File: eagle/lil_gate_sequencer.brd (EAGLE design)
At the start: 100 x 80 mm, 68 parts, among them IC1 4093N, IC2 4017N, Q1 2N3904, Q2 2N3904

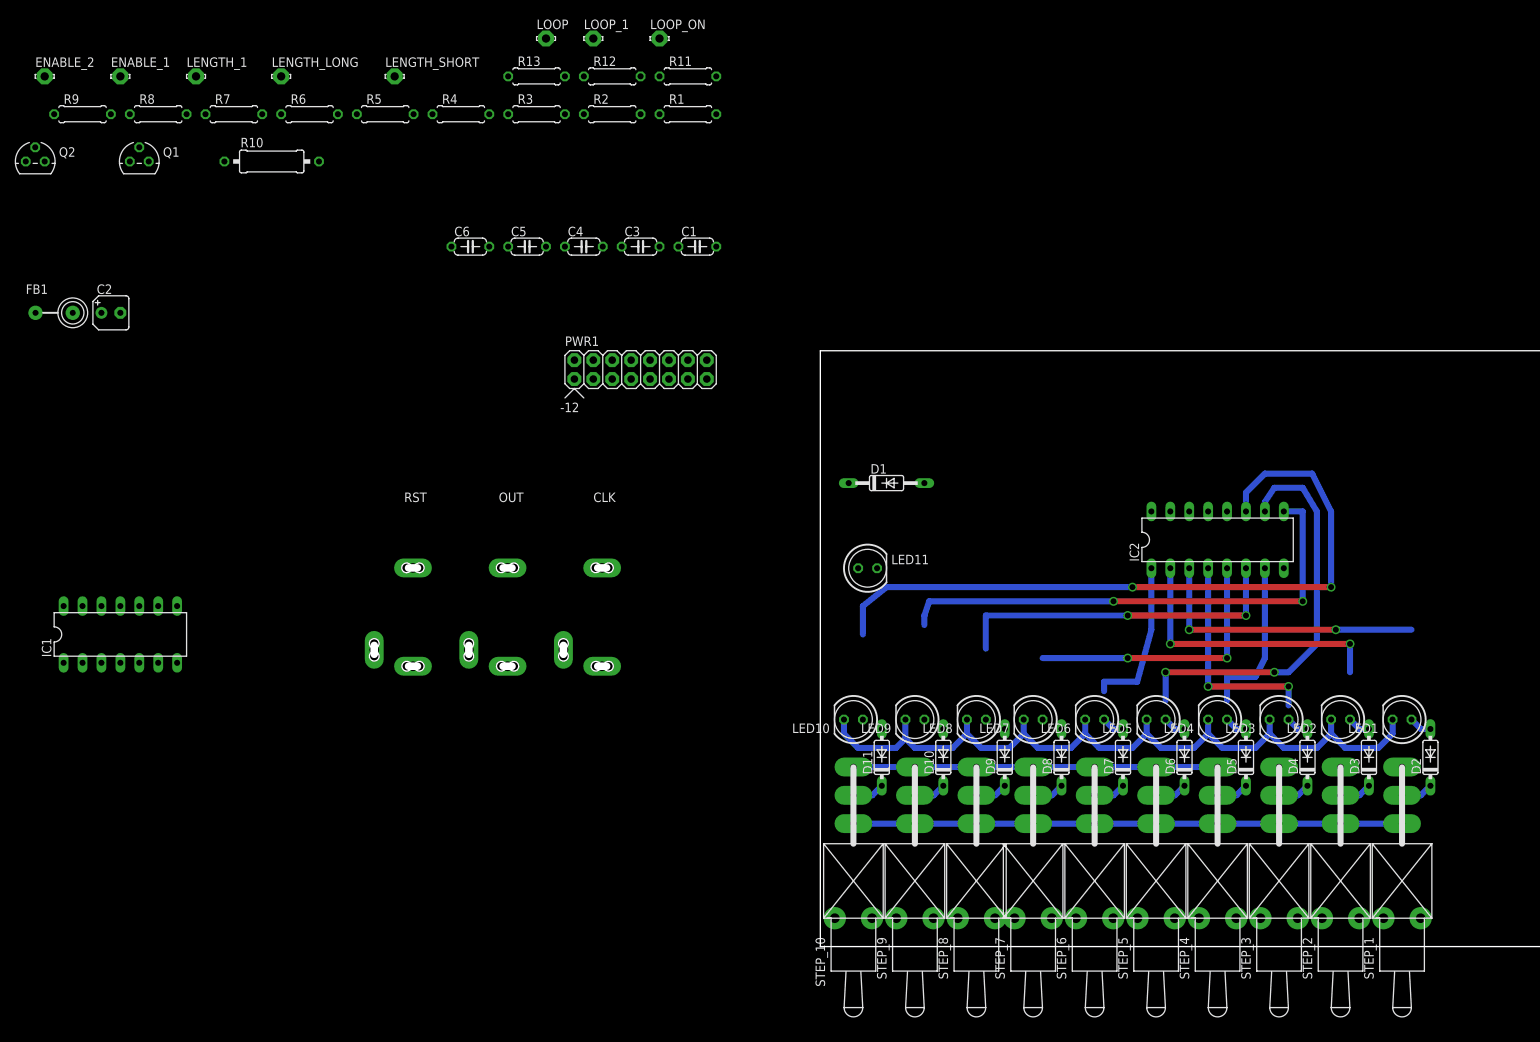
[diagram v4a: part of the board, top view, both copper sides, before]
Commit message: 4017 routed and adjusted
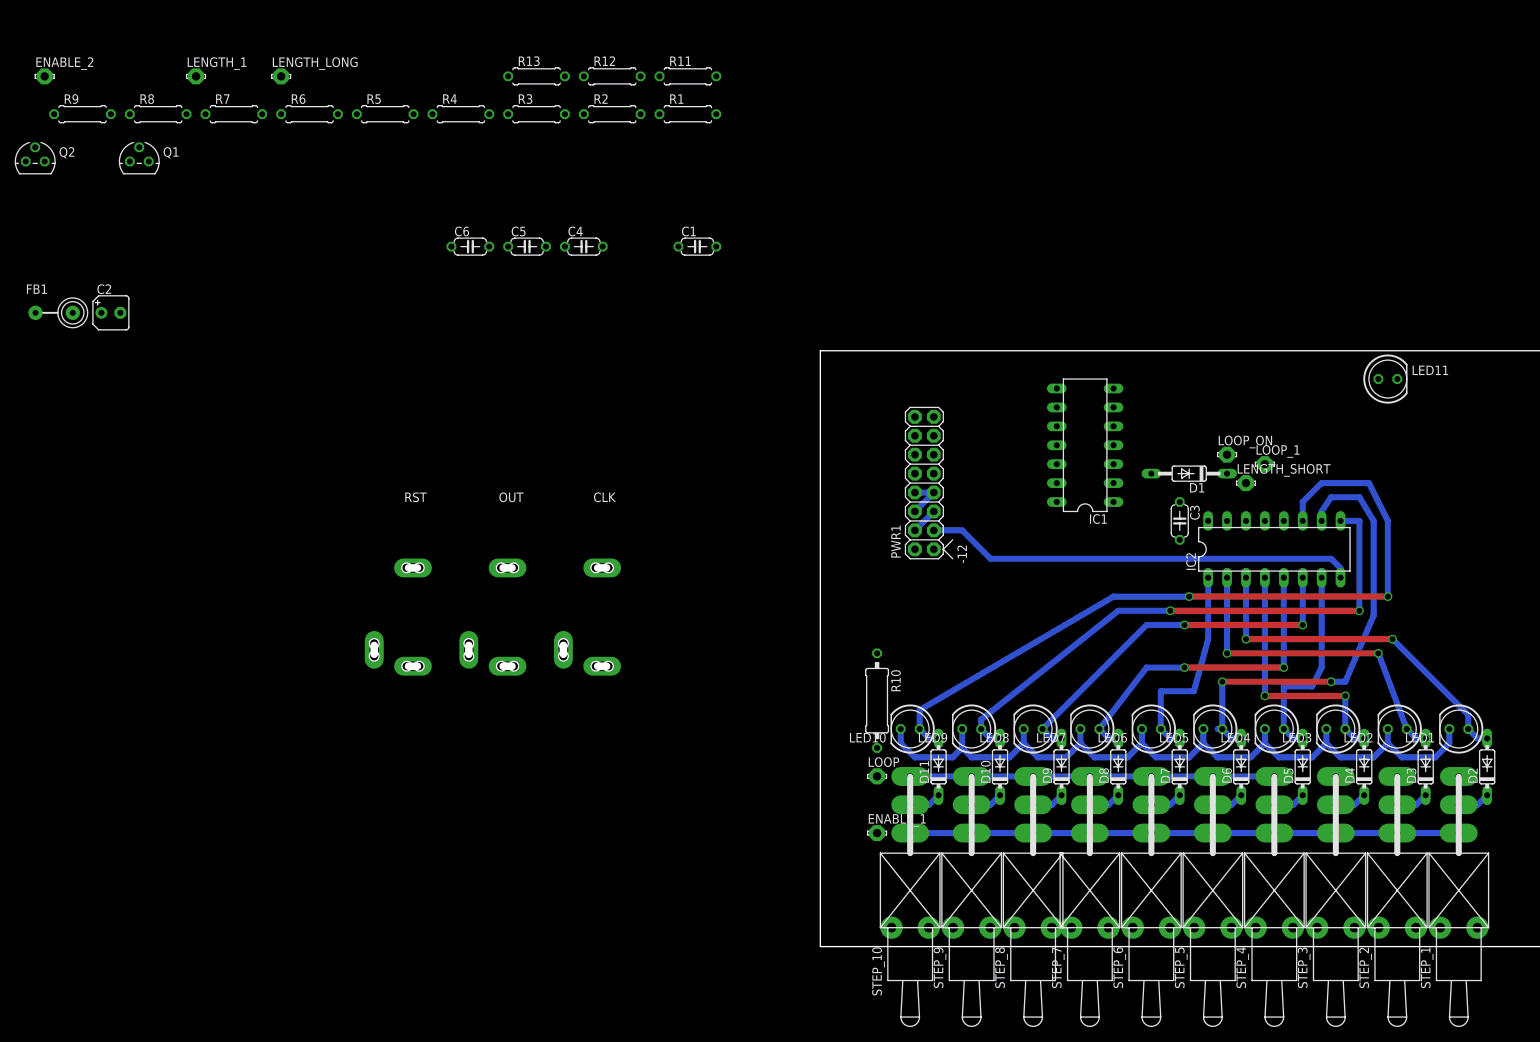
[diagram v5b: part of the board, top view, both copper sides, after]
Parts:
- moved ENABLE_1 143.7 mm to (7.62, 15.2)
- moved IC1 132.0 mm to (35.6, 67.3), turned to 90 degrees
- moved LENGTH_SHORT 126.7 mm to (57.1, 62.2)
- moved R10 108.8 mm to (7.62, 33.0), turned to 270 degrees
- moved LOOP 108.6 mm to (7.62, 22.9)
- moved LOOP_1 106.8 mm to (59.7, 64.8)
- moved LOOP_ON 94.5 mm to (54.6, 66.0)
- moved C3 81.2 mm to (48.3, 57.1), turned to 270 degrees
- moved LED11 74.3 mm to (76.2, 76.2)
- moved PWR1 44.4 mm to (14.0, 59.7), turned to 90 degrees
- moved D1 40.7 mm to (49.5, 63.5), turned to 180 degrees
- moved D3 7.73 mm to (81.3, 24.1)
- moved D4 7.73 mm to (73.0, 24.1)
- moved D8 7.73 mm to (40.0, 24.1)
- moved LED2 7.73 mm to (77.5, 29.2)
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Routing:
- net GND: track 0.00 -> 67.7 mm
- net N$27: track 36.8 -> 44.0 mm
- net N$31: track 68.0 -> 74.8 mm
- net N$15: track 41.2 -> 47.3 mm
- net N$33: track 95.9 -> 100.9 mm
- net N$29: track 45.7 -> 50.1 mm
- net N$25: track 24.3 -> 28.1 mm
- net N$17: track 41.2 -> 44.4 mm
- net N$21: track 25.0 -> 27.5 mm
- net N$23: track 57.6 -> 60.0 mm
- net N$19: track 32.3 -> 34.2 mm

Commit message: more routes
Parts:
- R10: device rcl:0309/12 -> rcl:0207/7
- moved Q2 177.5 mm to (69.8, 77.5), turned to 180 degrees
- moved R9 172.5 mm to (67.3, 66.0), turned to 180 degrees
- moved Q1 172.2 mm to (76.2, 66.0), turned to 180 degrees
- moved RST 162.0 mm to (100.3, 78.7), turned to 270 degrees
- moved R8 157.7 mm to (63.5, 71.1), turned to 180 degrees
- moved R7 139.9 mm to (55.9, 73.7)
- moved ENABLE_2 138.6 mm to (27.9, 74.9)
- moved CLK 135.3 mm to (100.3, 67.3), turned to 270 degrees
- moved LENGTH_LONG 132.8 mm to (50.8, 67.3)
- moved R4 130.7 mm to (77.5, 76.2), turned to 180 degrees
- moved R3 127.8 mm to (81.3, 66.0), turned to 270 degrees
- moved FB1 126.3 mm to (20.3, 57.1)
- moved R6 122.5 mm to (47.0, 71.1), turned to 270 degrees
- moved C2 118.1 mm to (20.3, 61.0)
- moved R1 116.0 mm to (83.8, 55.9)
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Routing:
- net GND: track 67.7 -> 440.3 mm
- net +12V: track 0.00 -> 50.8 mm
- net N$12: track 0.00 -> 31.6 mm
- net N$11: track 0.00 -> 26.2 mm
- net N$10: track 0.00 -> 22.4 mm
- net N$9: track 0.00 -> 17.1 mm
- net N$4: track 0.00 -> 13.1 mm
- net N$38: track 0.00 -> 12.5 mm
- net N$42: track 0.00 -> 11.2 mm
- net N$41: track 0.00 -> 11.0 mm
- net N$14: track 0.00 -> 10.5 mm
- net N$3: track 0.00 -> 7.92 mm
- net N$7: track 0.00 -> 7.67 mm
- net N$1: track 0.00 -> 7.66 mm
- net N$5: track 0.00 -> 6.88 mm
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
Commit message: routed
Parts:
- removed LED11: (no value), led:LED5MM
- added JP1: M02LOCK_LONGPADS, SparkFun-Connectors:1X02_LOCK_LONGPADS
- added OUT_LED, OUT_LED1: LSP11, solpad:LSP11
- moved OUT 72.7 mm to (6.35, 0.00), turned to 180 degrees
- moved CLK 67.3 mm to (100.3, 0.00), turned to 180 degrees
- moved R1 34.5 mm to (94.0, 22.9), turned to 270 degrees
- moved R13 21.1 mm to (8.89, 41.9), turned to 0 degrees
- moved C3 17.3 mm to (49.5, 53.3), turned to 270 degrees
- moved LENGTH_SHORT 11.5 mm to (47.0, 59.7)
- moved C4 11.4 mm to (25.4, 74.9), turned to 90 degrees
- moved C2 6.35 mm to (25.4, 57.1), turned to 90 degrees
- moved LOOP_ON 5.08 mm to (59.7, 66.0)
- moved FB1 4.02 mm to (19.1, 53.3)
- moved LENGTH_1 2.84 mm to (20.3, 74.9)
- moved LOOP_1 2.84 mm to (59.7, 61.0)
- moved C1 2.84 mm to (50.8, 74.9), turned to 270 degrees
- moved ENABLE_1 2.54 mm to (7.62, 17.8)
- moved PWR1 2.54 mm to (8.89, 53.3)
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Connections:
- new net N$39: JP1.1, PWR1.15, PWR1.16
- net N$43: now also OUT_LED1.MP; no longer LED11.K
- net N$6: now also JP1.2, OUT_LED.MP; no longer LED11.A
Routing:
- net N$6: track 0.00 -> 93.9 mm, vias 0 -> 2
- net N$5: track 6.88 -> 81.1 mm
- net N$4: track 13.1 -> 42.8 mm
- net +12V: track 50.8 -> 73.3 mm, vias 0 -> 2
- net N$34: track 48.9 -> 70.5 mm
- net N$39: track 0.00 -> 8.55 mm
- net N$36: track 73.7 -> 78.8 mm
- net N$41: track 11.0 -> 6.43 mm
- net N$43: track 0.00 -> 4.34 mm
- net GND: track 440.3 -> 436.1 mm, vias 0 -> 2
- net N$7: track 7.67 -> 4.02 mm
- net N$11: track 26.2 -> 22.7 mm
- net N$1: track 7.66 -> 10.5 mm
- net N$21: track 27.5 -> 24.9 mm
- net N$25: track 28.1 -> 26.0 mm
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
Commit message: reversed
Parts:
- moved LOOP 84.6 mm to (92.1, 27.3)
- moved ENABLE_1 83.8 mm to (91.4, 19.1)
- moved D2 74.3 mm to (15.2, 26.7)
- moved LED1 74.3 mm to (11.4, 31.8)
- moved STEP_1 74.3 mm to (11.4, 5.08)
- moved D11 73.7 mm to (89.5, 26.7)
- moved LED10 73.7 mm to (85.7, 31.8)
- moved STEP_10 73.7 mm to (85.7, 5.08)
- moved D3 57.8 mm to (23.5, 26.7)
- moved LED2 57.8 mm to (19.7, 31.8)
- moved STEP_2 57.8 mm to (19.7, 5.08)
- moved D10 57.2 mm to (81.3, 26.7)
- moved LED9 57.2 mm to (77.5, 31.8)
- moved STEP_9 57.2 mm to (77.5, 5.08)
- moved D4 41.4 mm to (31.8, 26.7)
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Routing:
- net N$35: track 112.0 -> 4.86 mm
- net N$33: track 101.1 -> 3.07 mm, vias 2 -> 0
- net N$31: track 74.8 -> 3.07 mm, vias 2 -> 0
- net N$23: track 59.6 -> 3.07 mm, vias 2 -> 0
- net N$29: track 50.1 -> 3.07 mm, vias 2 -> 0
- net N$15: track 47.3 -> 3.07 mm, vias 2 -> 0
- net N$17: track 44.4 -> 3.07 mm, vias 2 -> 0
- net N$27: track 44.0 -> 3.07 mm, vias 2 -> 0
- net N$19: track 34.2 -> 3.07 mm, vias 2 -> 0
- net N$25: track 26.0 -> 3.07 mm
- net N$21: track 24.9 -> 3.70 mm
- net N$7: track 4.02 -> 18.0 mm
- net N$4: track 42.8 -> 30.2 mm
- net N$34: track 70.5 -> 73.9 mm
- net N$36: track 78.8 -> 80.5 mm
